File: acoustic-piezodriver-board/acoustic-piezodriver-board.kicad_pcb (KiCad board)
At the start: 4 copper layers, 100 x 62 mm, 158 parts, among them J301 Conn_02x06_Odd_Even, J501 Conn_02x06_Odd_Even, P101 WJ128V-5.0-3P, P201 WJ128V-5.0-3P, Q501 AO3400A, Q502 AO3400A, U10 NCE6005AS, U101 AMS1117-3.3, U102 D0008A-IPC_A, U201 UCC27282DR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

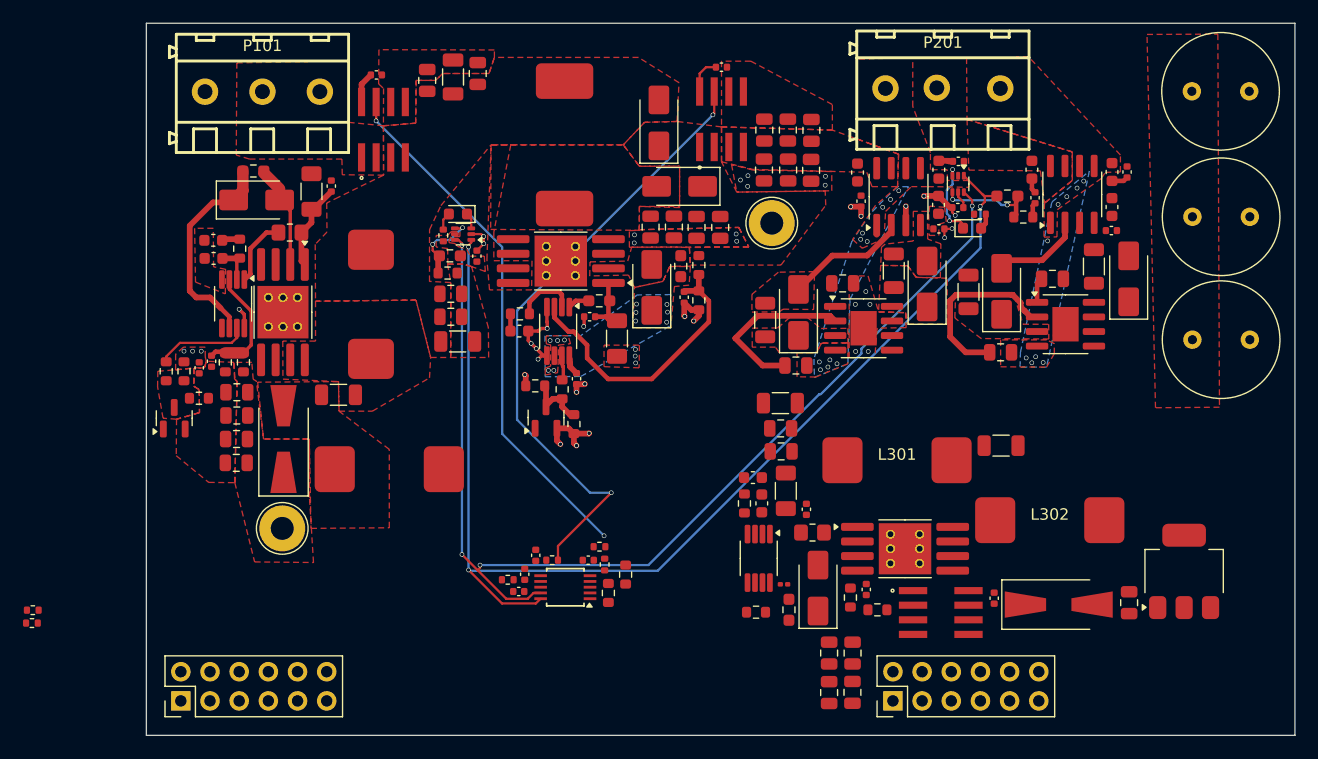
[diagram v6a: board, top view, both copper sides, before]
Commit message: main routing completed, finish 3V3 + I2C bus
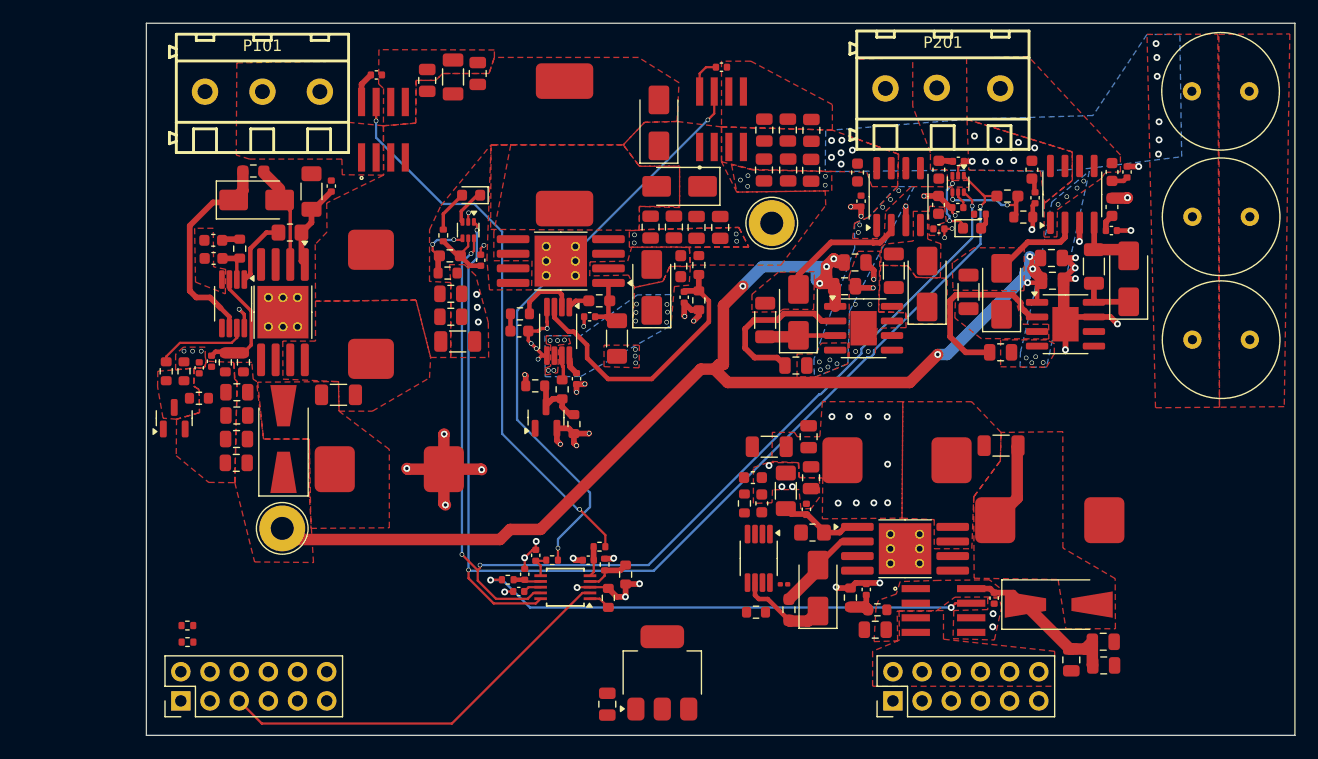
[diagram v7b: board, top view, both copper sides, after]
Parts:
- added C211: 1uF, Capacitor_SMD:C_0805_2012Metric, F.Cu at (105.7, 100.8)
- added C212: 1uF, Capacitor_SMD:C_0805_2012Metric, F.Cu at (122.8, 100.4)
- U102: value D0008A-IPC_A -> TMCS1108A3UQDR
- moved C101 46.3 mm to (84.1, 139.3)
- moved U101 46.3 mm to (88.9, 136.6)
- moved C41 22.0 mm to (127.3, 135.9), turned to 0 degrees
- moved C40 21.8 mm to (127.3, 133.8), turned to 0 degrees
- moved C42 21.3 mm to (124.5, 135.4)
- moved R404 13.6 mm to (47.6, 133.9), turned to 0 degrees
- moved R403 13.5 mm to (47.6, 132.4)
- moved C43 4.50 mm to (107.5, 132.8), turned to 180 degrees
- moved C34 3.92 mm to (98.2, 116.9)
- moved C35 3.47 mm to (101.9, 119.6), turned to -90 degrees
- moved C36 2.54 mm to (101.7, 116.0), turned to 90 degrees
- moved D401 2.00 mm to (72.3, 95.0)
- moved U402 0.57 mm to (72.0, 98.0), turned to -90 degrees
- moved C401 0.49 mm to (73.1, 100.6)
- moved R411 0.43 mm to (84.2, 130.0)
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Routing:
- net /INVERTER/10V: track 2.21 -> 110.7 mm, vias 0 -> 8
- net GND: track 31.8 -> 88.0 mm, vias 38 -> 71
- net /COMPUTE_POWER/ADC_IFPGA: track 0.00 -> 44.0 mm, vias 0 -> 2
- net /SENSORS_CONN/ADC_ALERT: track 0.00 -> 36.1 mm
- net +6V: track 5.91 -> 21.0 mm
- net Net-(D5-A): track 0.00 -> 8.31 mm
- net Net-(D5-K): track 0.00 -> 7.88 mm
- net Net-(U10B-S2): track 0.00 -> 7.37 mm
- net Net-(D2-A): track 0.00 -> 7.31 mm
- net +3V3: track 1.88 -> 9.07 mm
- net Net-(D8-K): track 0.00 -> 6.15 mm
- net Net-(D10-A): track 0.00 -> 5.62 mm
- net Net-(D10-K): track 0.00 -> 4.71 mm
- net /SENSORS_CONN/ADC_VBAT: track 0.00 -> 3.96 mm
- net Net-(U9-FB): track 0.00 -> 2.98 mm
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- added copper zone on F.Cu, net +6V
- added copper zone on F.Cu, net /COMPUTE_POWER/6V_N
- added copper zone on B.Cu, net /INVERTER/VINV_N
- added copper zone on F.Cu, net Net-(C38-Pad1)
- added copper zone on F.Cu, net Net-(D11-A)
- added copper zone on F.Cu, net Net-(D2-A)
- removed copper zone on F.Cu, net +3V3
- removed copper zone on F.Cu, net Net-(D8-K)

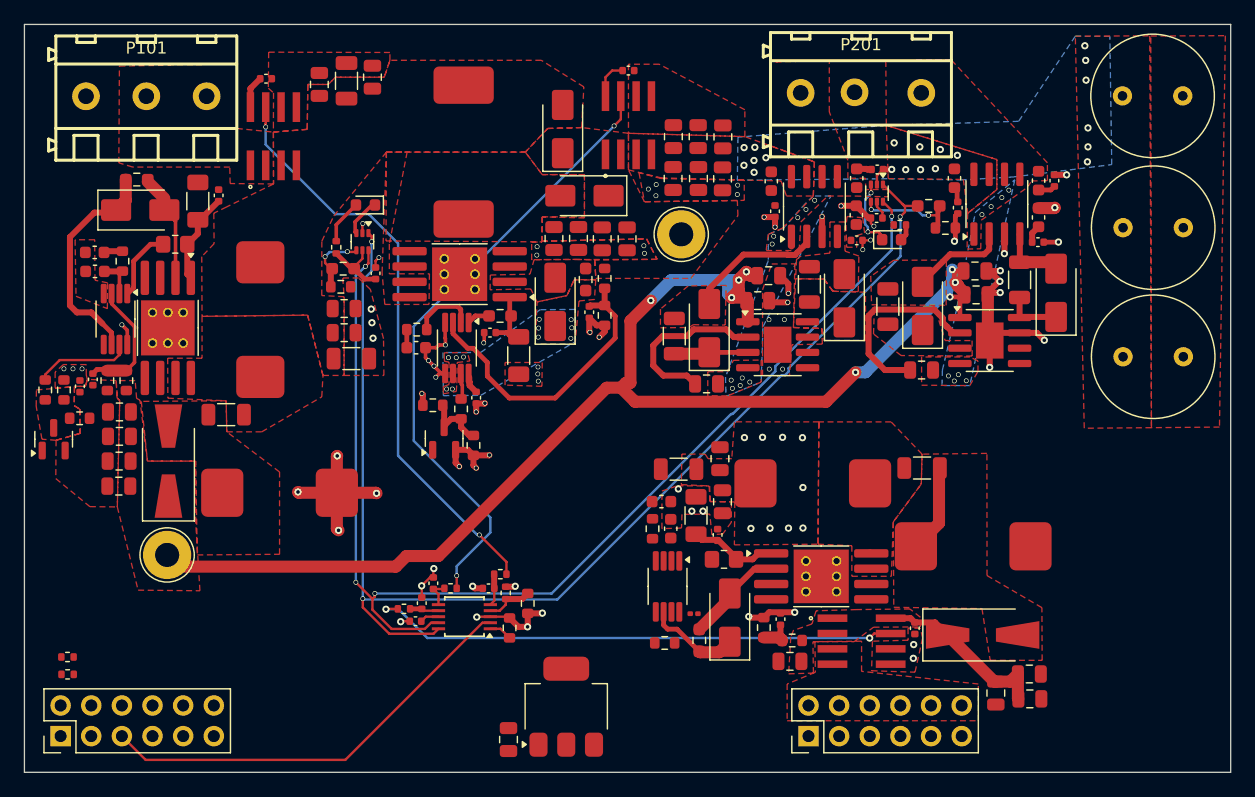
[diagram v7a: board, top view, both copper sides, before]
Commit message: completed 3V3 routing
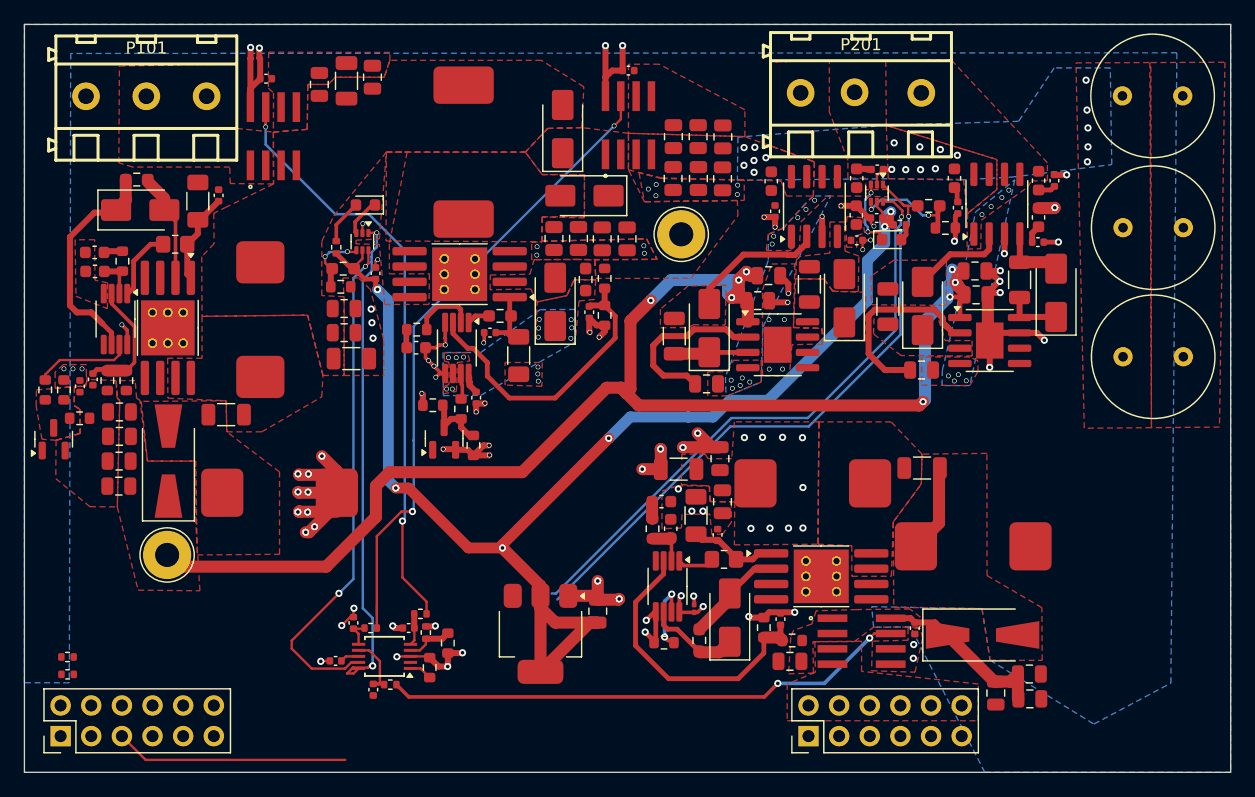
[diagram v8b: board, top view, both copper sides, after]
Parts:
- moved C101 13.0 mm to (91.5, 128.6), turned to 90 degrees
- moved C406 8.22 mm to (72.9, 135.2), turned to -90 degrees
- moved C405 7.40 mm to (71.3, 129.6)
- moved R409 7.40 mm to (76.8, 128.9)
- moved C404 7.40 mm to (69.8, 132.8)
- moved R410 7.40 mm to (72.7, 130.0)
- moved R413 7.40 mm to (77.3, 130.4)
- moved C402 7.40 mm to (75.9, 130.0)
- moved R411 7.40 mm to (77.6, 133.3)
- moved R412 7.40 mm to (79.1, 131.3)
- moved U404 7.40 mm to (73.9, 132.4)
- moved U101 6.41 mm to (86.8, 130.5), turned to -90 degrees
- moved R414 6.38 mm to (74.3, 134.7), turned to 180 degrees
- moved C301 0.43 mm to (99.5, 128.4), turned to 90 degrees
- moved R18 0.07 mm to (97.0, 131.2)
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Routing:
- net +3V3: track 9.07 -> 113.5 mm, vias 0 -> 6
- net GND: track 88.0 -> 111.9 mm, vias 71 -> 85
- net Net-(U9-FB): track 2.98 -> 24.9 mm
- net /SENSORS_CONN/ADC_ALERT: track 36.1 -> 19.3 mm
- net +6V: track 21.0 -> 33.2 mm, vias 0 -> 4
- net /SENSORS_CONN/T_SCL: track 103.5 -> 93.6 mm
- net /INVERTER/10V: track 110.7 -> 117.4 mm
- net Net-(U9-FA/SD): track 0.00 -> 6.24 mm, vias 0 -> 2
- net /SENSORS_CONN/T_SDA: track 96.9 -> 91.7 mm, vias 4 -> 3
- net +BATT: track 5.09 -> 8.69 mm, vias 15 -> 17
- net Net-(U9-COMP): track 0.00 -> 3.46 mm
- net Net-(U404-AIN3): track 2.41 -> 5.50 mm
- net Net-(U9-I_{SEN}): track 0.00 -> 3.08 mm
- net /INVERTER/ADC_IINV: track 53.7 -> 55.9 mm
- net Net-(C32-Pad1): track 0.00 -> 1.44 mm
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- added copper zone on B.Cu, net +6V
